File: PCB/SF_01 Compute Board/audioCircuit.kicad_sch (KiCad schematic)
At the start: 136 parts, among them J10 SUBWOOFER_6, J5 SUBWOOFER_1, J6 SUBWOOFER_2, J7 SUBWOOFER_3, J8 SUBWOOFER_4, J9 SUBWOOFER_5, U17 TPA3116D2DAD, U18 TPA3116D2DAD, U19 TPA3116D2DAD

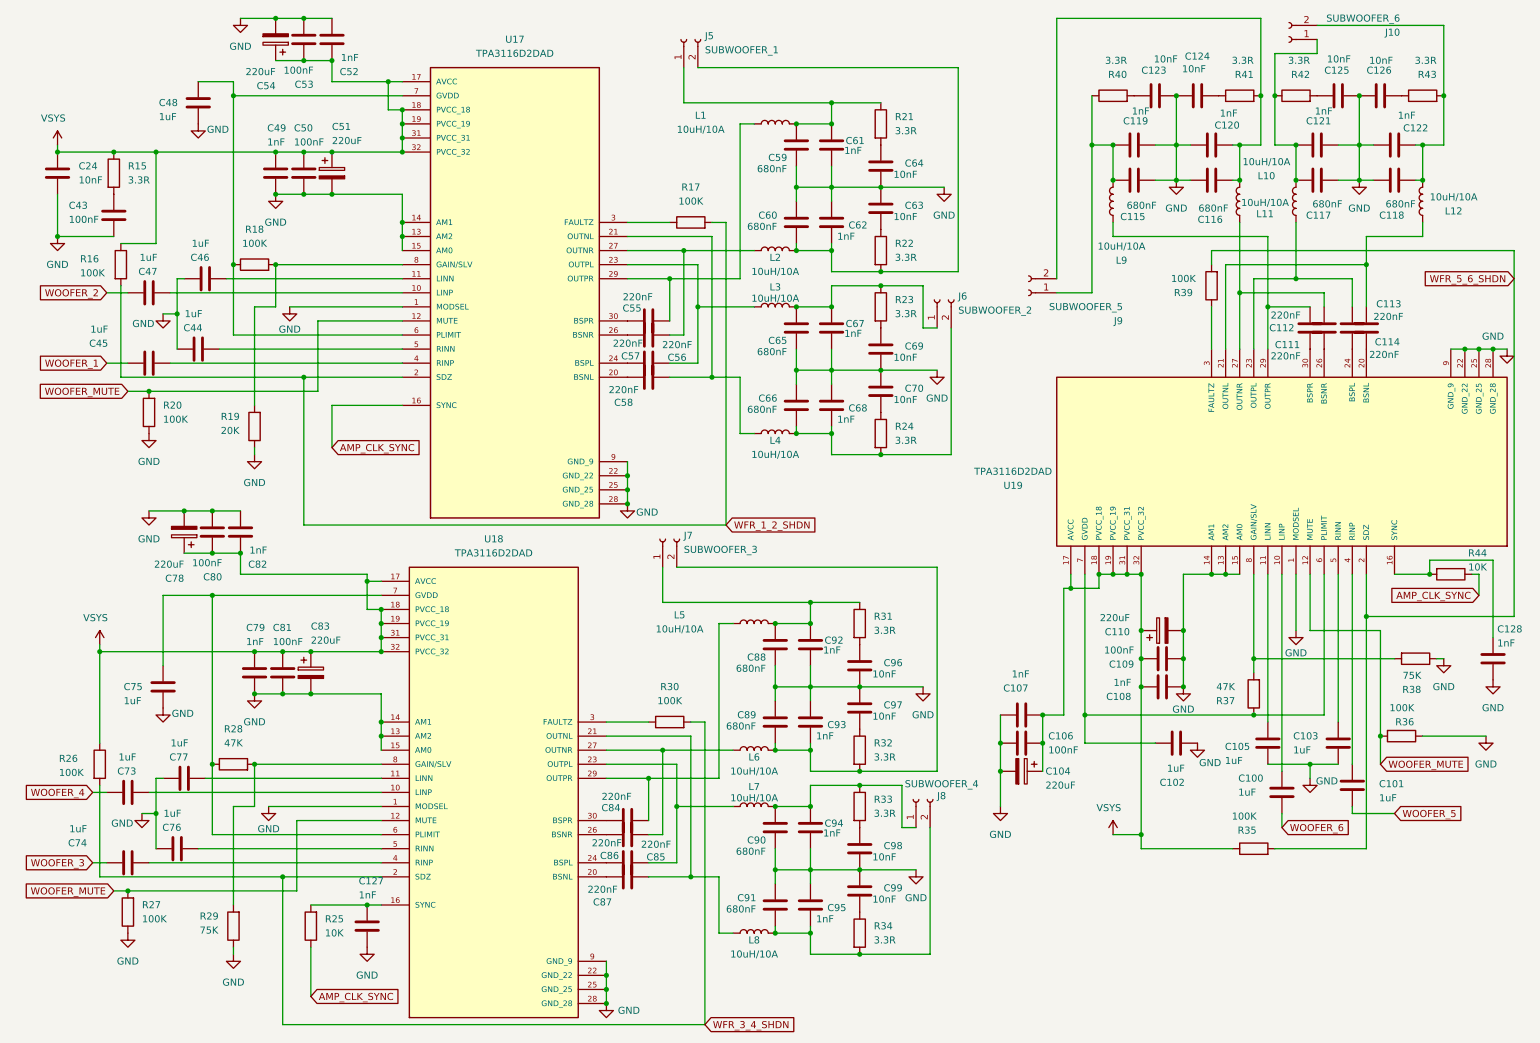
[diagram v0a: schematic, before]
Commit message: Changed Audio Multiplexer Circuit, Routed more
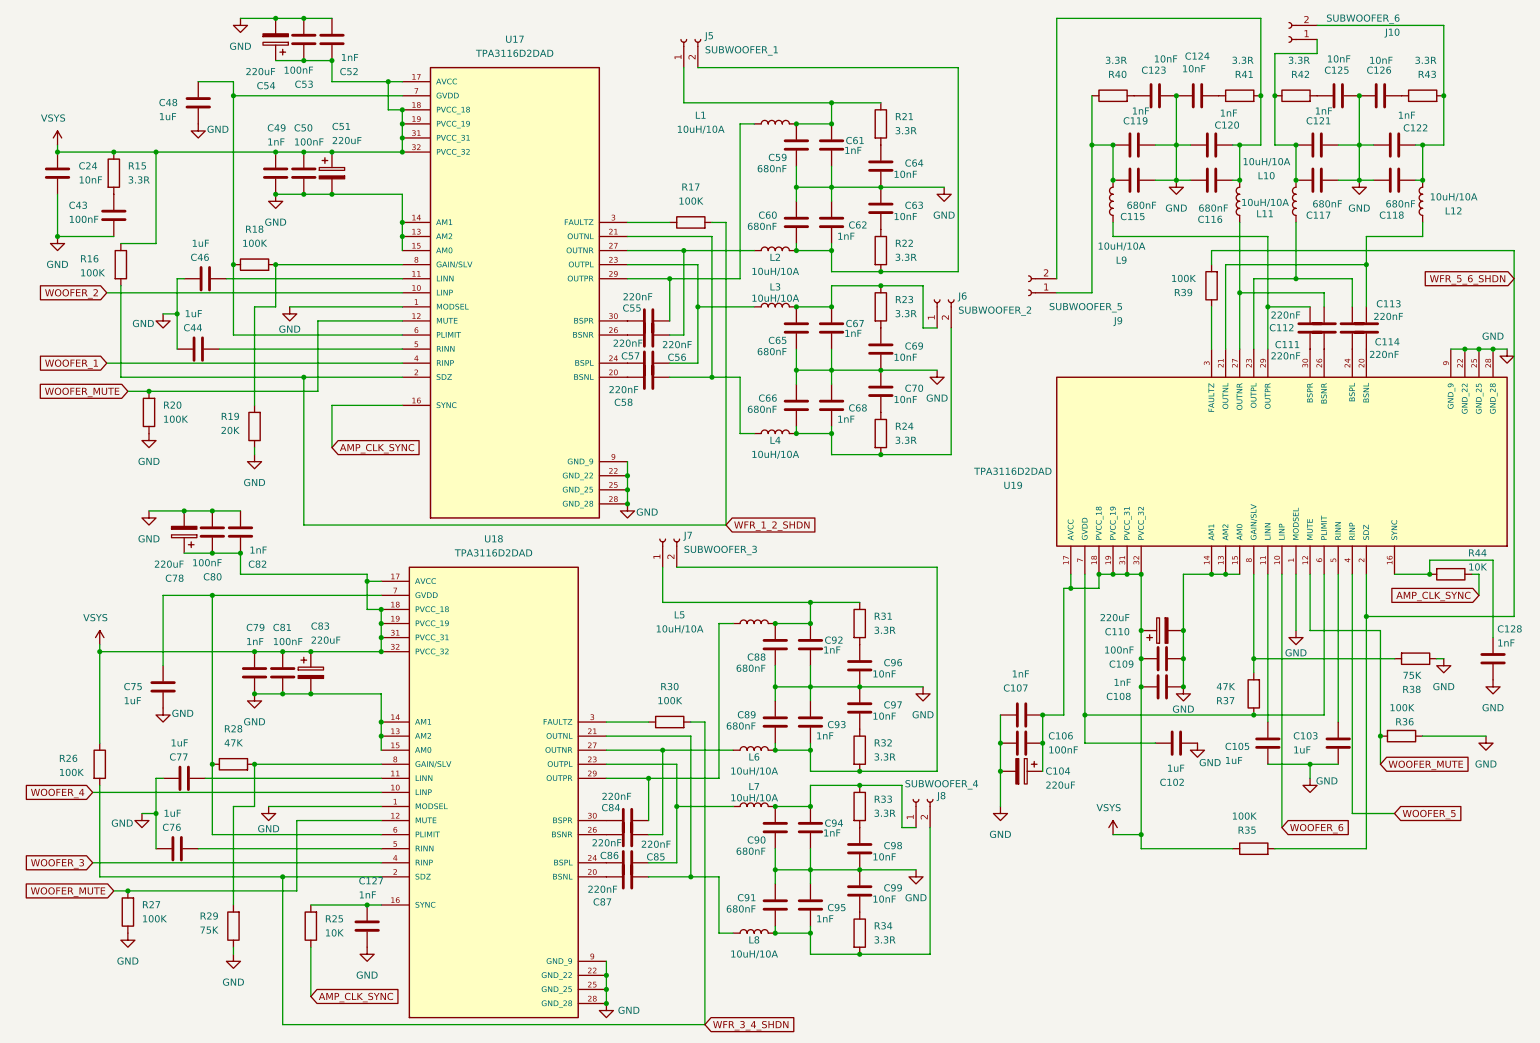
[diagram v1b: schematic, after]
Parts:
- removed C100, C101, C45, C47, C73, C74: 1uF, Capacitor_SMD:C_0603_1608Metric, symbol Device:C
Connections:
- net WOOFER_1: now also U17.4 (RINP)
- net WOOFER_2: now also U17.10 (LINP)
- net WOOFER_3: now also U18.4 (RINP)
- net WOOFER_4: now also U18.10 (LINP)
- net WOOFER_5: now also U19.4 (RINP)
- net WOOFER_6: now also U19.10 (LINP)

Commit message: Added USB Host control, Routed 1st amplifier
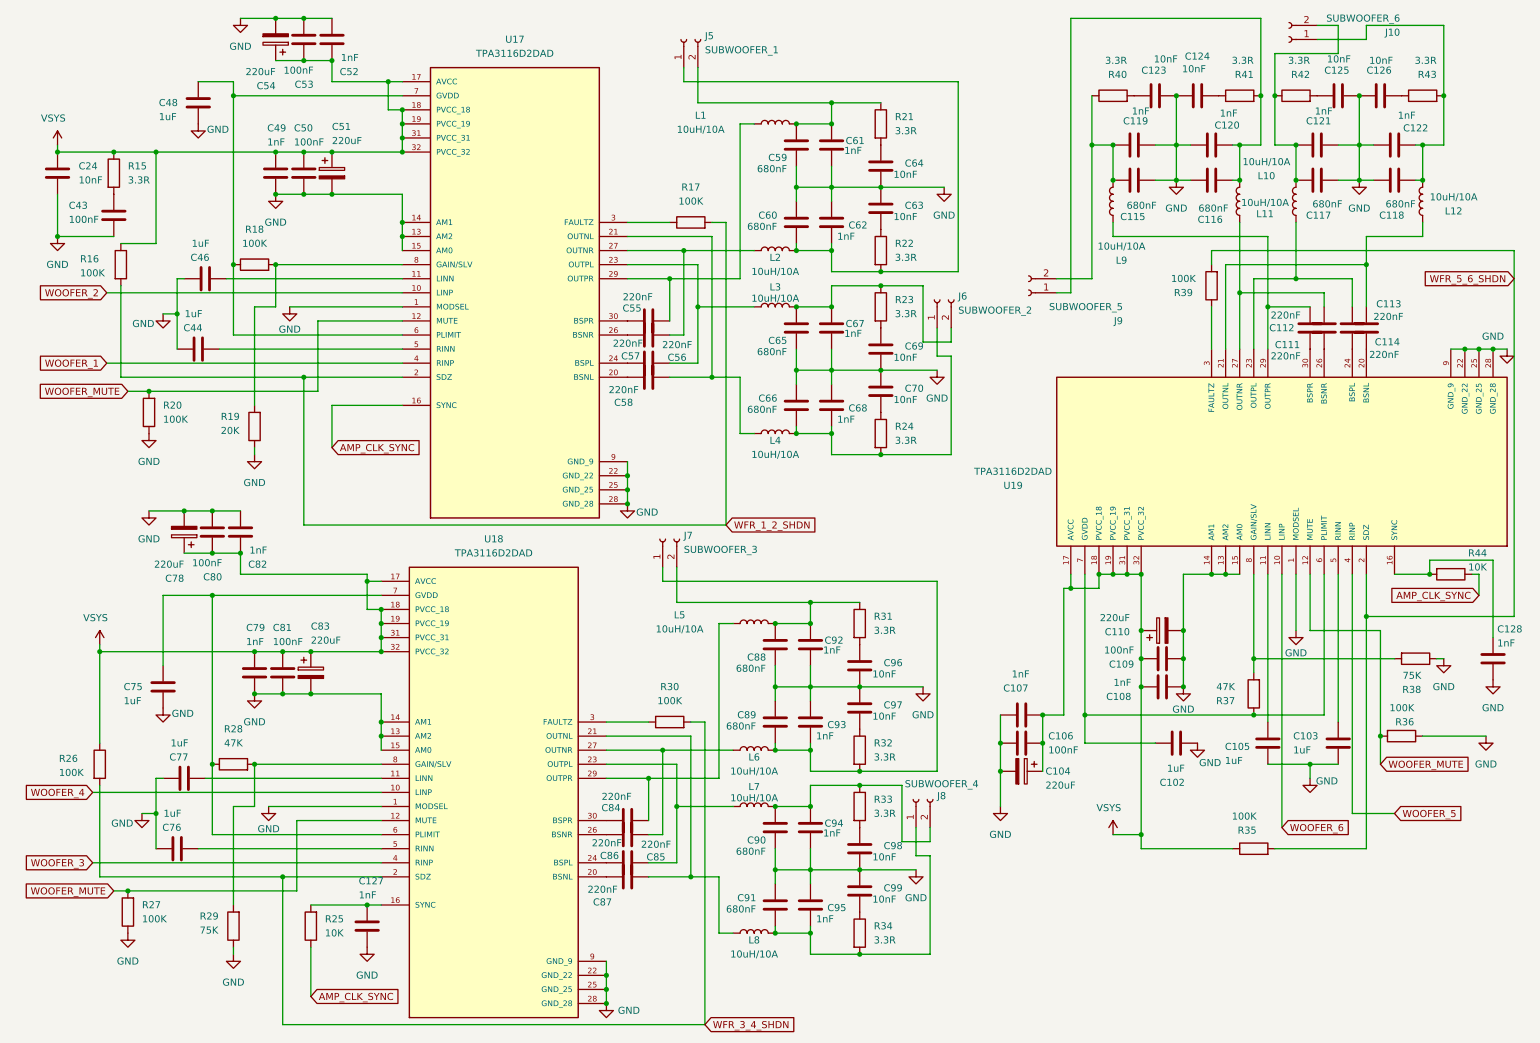
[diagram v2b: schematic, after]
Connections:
- net at C117.2, C121.2, L11.2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: now also J10.2 (Pin_2); no longer J10.1 (Pin_1)
- net at C66.1, C68.1, L4.2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: now also J6.1 (Pin_1); no longer J6.2 (Pin_2)
- net at C88.2, C92.2, L5.2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: now also J7.2 (Pin_2); no longer J7.1 (Pin_1)
- net at C116.1, C120.1, L10.2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: now also J9.1 (Pin_1); no longer J9.2 (Pin_2)
- net at C89.1, C93.1, L6.2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: now also J7.1 (Pin_1); no longer J7.2 (Pin_2)
- net at C59.2, C61.2, L1.2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: now also J5.2 (Pin_2); no longer J5.1 (Pin_1)
- net at C60.1, C62.1, L2.2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: now also J5.1 (Pin_1); no longer J5.2 (Pin_2)
- net at C65.2, C67.2, L3.2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: now also J6.2 (Pin_2); no longer J6.1 (Pin_1)
- net at C118.1, C122.1, L12.2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: now also J10.1 (Pin_1); no longer J10.2 (Pin_2)
- net at C115.2, C119.2, L9.2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: now also J9.2 (Pin_2); no longer J9.1 (Pin_1)
- net at C90.2, C94.2, L7.2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: now also J8.2 (Pin_2); no longer J8.1 (Pin_1)
- net at C91.1, C95.1, L8.2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: now also J8.1 (Pin_1); no longer J8.2 (Pin_2)

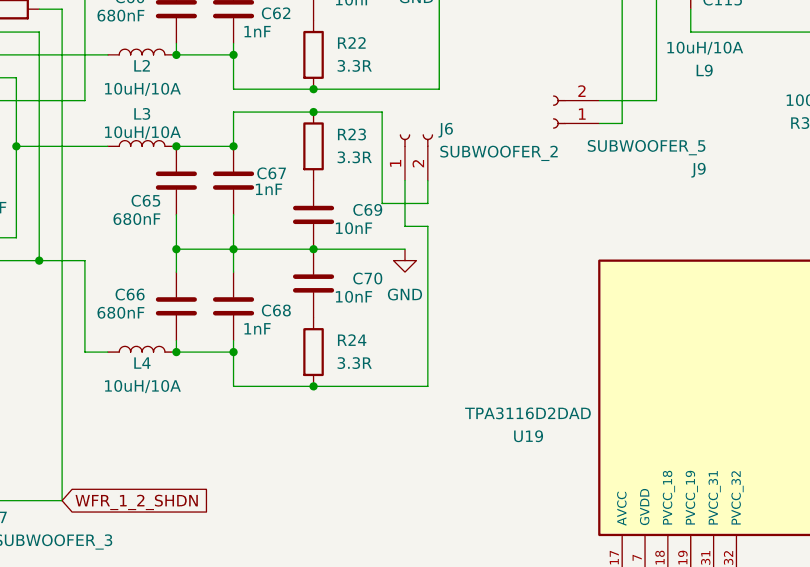
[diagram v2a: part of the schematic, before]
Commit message: Finished Routing 2nd Amplifier, started routing 3rd
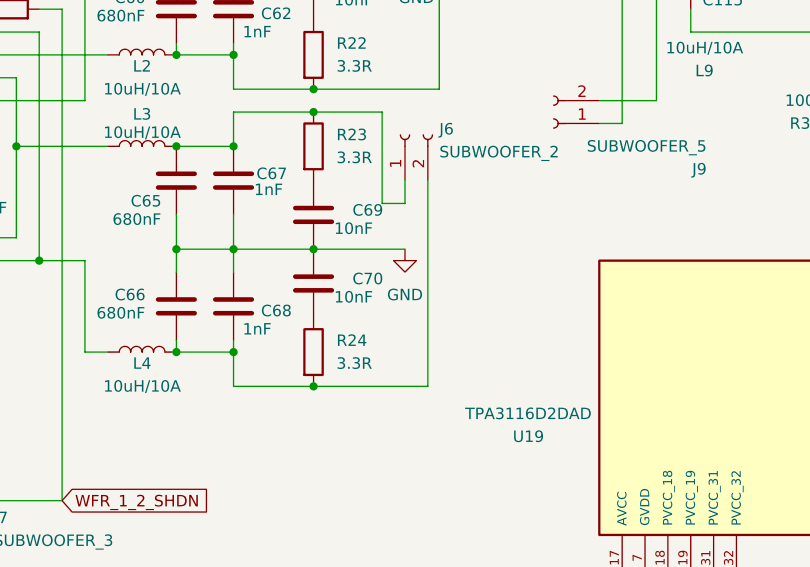
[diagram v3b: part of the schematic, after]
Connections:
- net at C66.1, C68.1, L4.2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: now also J6.2 (Pin_2); no longer J6.1 (Pin_1)
- net at C65.2, C67.2, L3.2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: now also J6.1 (Pin_1); no longer J6.2 (Pin_2)
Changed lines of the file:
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@@
-	(wire
-		(pts
-			(xy 180.34 69.85) (xy 180.34 72.39)
-		)
-		(stroke
-			(width 0)
-			(type default)
-		)
-	)
 	(wire
 		(pts
@@
 	(wire
 		(pts
-			(xy 180.34 74.93) (xy 180.34 92.71)
+			(xy 180.34 69.85) (xy 180.34 92.71)
 		)
 		(stroke
@@
 	(wire
 		(pts
-			(xy 177.8 69.85) (xy 177.8 74.93)
-		)
-		(stroke
-			(width 0)
-			(type default)
-		)
-	)
-	(wire
-		(pts
 			(xy 44.45 25.4) (xy 50.8 25.4)
 		)
@@
 	(wire
 		(pts
-			(xy 175.26 72.39) (xy 180.34 72.39)
-		)
-		(stroke
-			(width 0)
-			(type default)
-		)
-	)
-	(wire
-		(pts
 			(xy 54.61 66.04) (xy 54.61 83.82)
 		)
@@
 	(wire
 		(pts
-			(xy 177.8 74.93) (xy 180.34 74.93)
-		)
-		(stroke
-			(width 0)
-			(type default)
-		)
-	)
-	(wire
-		(pts
 			(xy 154.94 119.38) (xy 154.94 123.19)
 		)
@@
 	(wire
 		(pts
+			(xy 177.8 72.39) (xy 177.8 69.85)
+		)
+		(stroke
+			(width 0)
+			(type default)
+		)
+	)
+	(wire
+		(pts
 			(xy 240.03 114.3) (xy 240.03 160.02)
 		)
@@
 		)
 		(stroke
+			(width 0)
+			(type default)
+		)
+	)
+	(wire
+		(pts
+			(xy 175.26 72.39) (xy 177.8 72.39)
+		)
+		(stroke
